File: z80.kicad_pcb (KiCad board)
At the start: 2 copper layers, 97.2 x 111.8 mm, 35 parts, among them P2 CONN_01X02, P3 Jumper, SW1 RESET, U1 Z80CPU, U2 DIP_OSCILLATOR, U3 ATF16V8CV

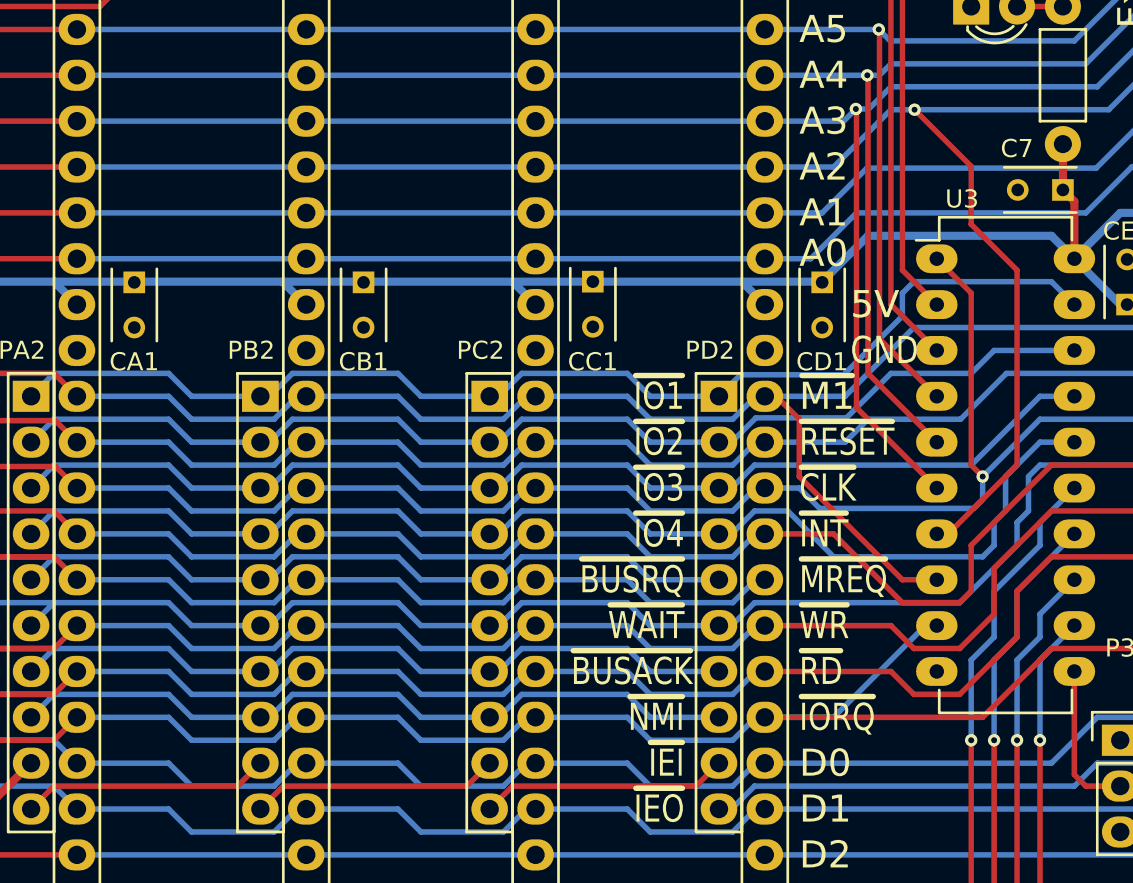
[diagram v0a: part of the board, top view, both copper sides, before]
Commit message: Added logo schematic elements and new logo for bottom side.
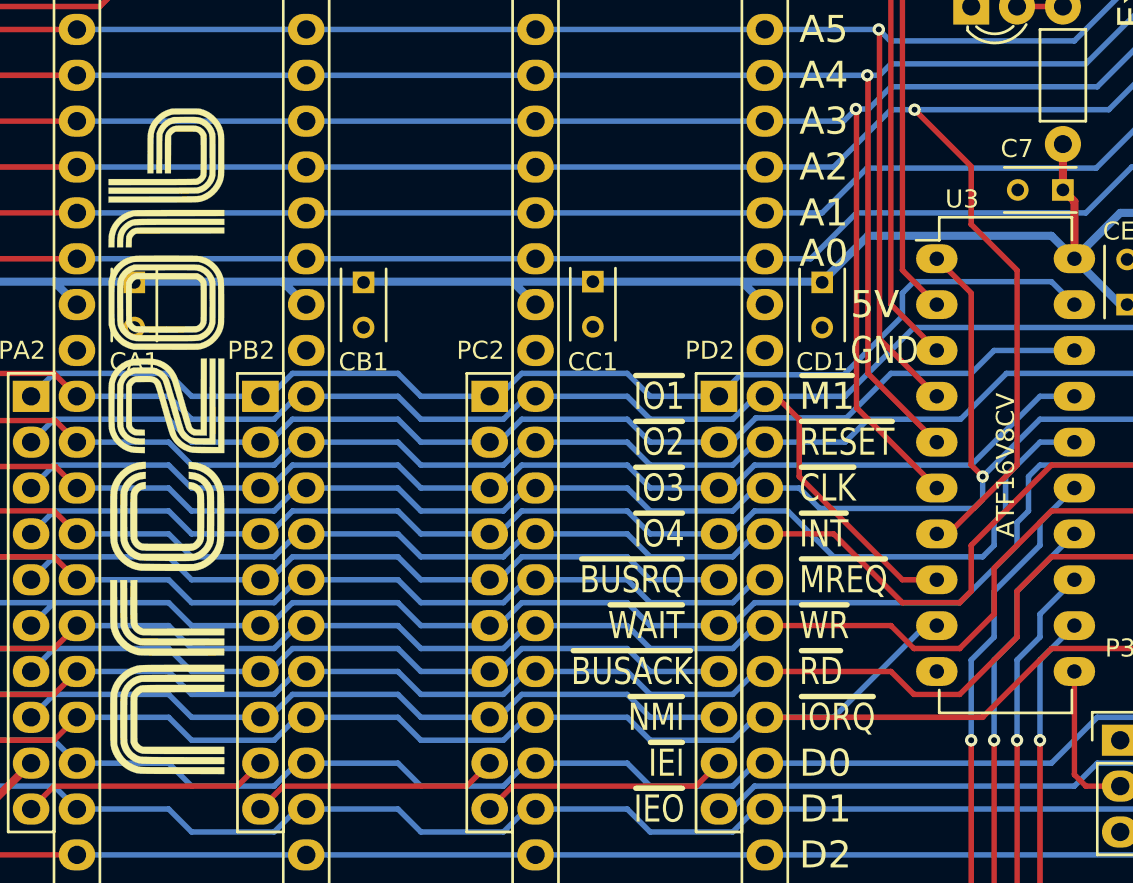
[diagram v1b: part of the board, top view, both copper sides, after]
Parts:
- added LOGO1: FrontLogo, ncr2016_logo:nrc2016_top_logo_1600, F.Cu at (78.7, 86.4)
- added LOGO2: BackLogo, ncr2016_logo:nrc2016_bottom_logo_600, B.Cu at (89.5, 85.1)
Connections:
- net /A0 renamed /CPU/A0
- net /A1 renamed /CPU/A1
- net /A10 renamed /CPU/A10
- net /A11 renamed /CPU/A11
- net /A12 renamed /CPU/A12
- net /A13 renamed /CPU/A13
- net /A14 renamed /CPU/A14
- net /A15 renamed /CPU/A15
- net /A2 renamed /CPU/A2
- net /A3 renamed /CPU/A3
- net /A4 renamed /CPU/A4
- net /A5 renamed /CPU/A5
- net /A6 renamed /CPU/A6
- net /A7 renamed /CPU/A7
- net /A8 renamed /CPU/A8
- net /A9 renamed /CPU/A9
- net /Card Slots/RX renamed /Card Slots/Expansion/RX
- net /Card Slots/S1 renamed /Card Slots/Expansion/SPARE1
- net /Card Slots/S2 renamed /Card Slots/Expansion/SPARE2
- net /Card Slots/S3 renamed /Card Slots/Expansion/SPARE3
- net /Card Slots/S4 renamed /Card Slots/PortA/SPARE4
- net /Card Slots/TX renamed /Card Slots/Expansion/TX
- net /Card Slots/~IOSEL0 renamed /Card Slots/PortA/~IOSEL0
- net /Card Slots/~IOSEL1 renamed /Card Slots/PortA/~IOSEL1
- net /Card Slots/~IOSEL2 renamed /Card Slots/PortA/~IOSEL2
- net /Card Slots/~IOSEL3 renamed /Card Slots/PortA/~IOSEL3
- net /D0 renamed /CPU/D0
- net /D1 renamed /CPU/D1
- net /D2 renamed /CPU/D2
- net /D3 renamed /CPU/D3
- net /D4 renamed /CPU/D4
- net /D5 renamed /CPU/D5
- net /D6 renamed /CPU/D6
- net /D7 renamed /CPU/D7
- net /~BUSACK renamed /CPU/~BUSACK
- net /~BUSRQ renamed /CPU/~BUSRQ
- net /~CLK renamed /CPU/~CLK
- net /~INT renamed /CPU/~INT
- net /~IORQ renamed /CPU/~IORQ
- net /~M1 renamed /CPU/~M1
- net /~MREQ renamed /CPU/~MREQ
- net /~NMI renamed /CPU/~NMI
- net /~RD renamed /CPU/~RD
- net /~RESET renamed /CPU/~RESET
- net /~WAIT renamed /CPU/~WAIT
- net /~WR renamed /CPU/~WR

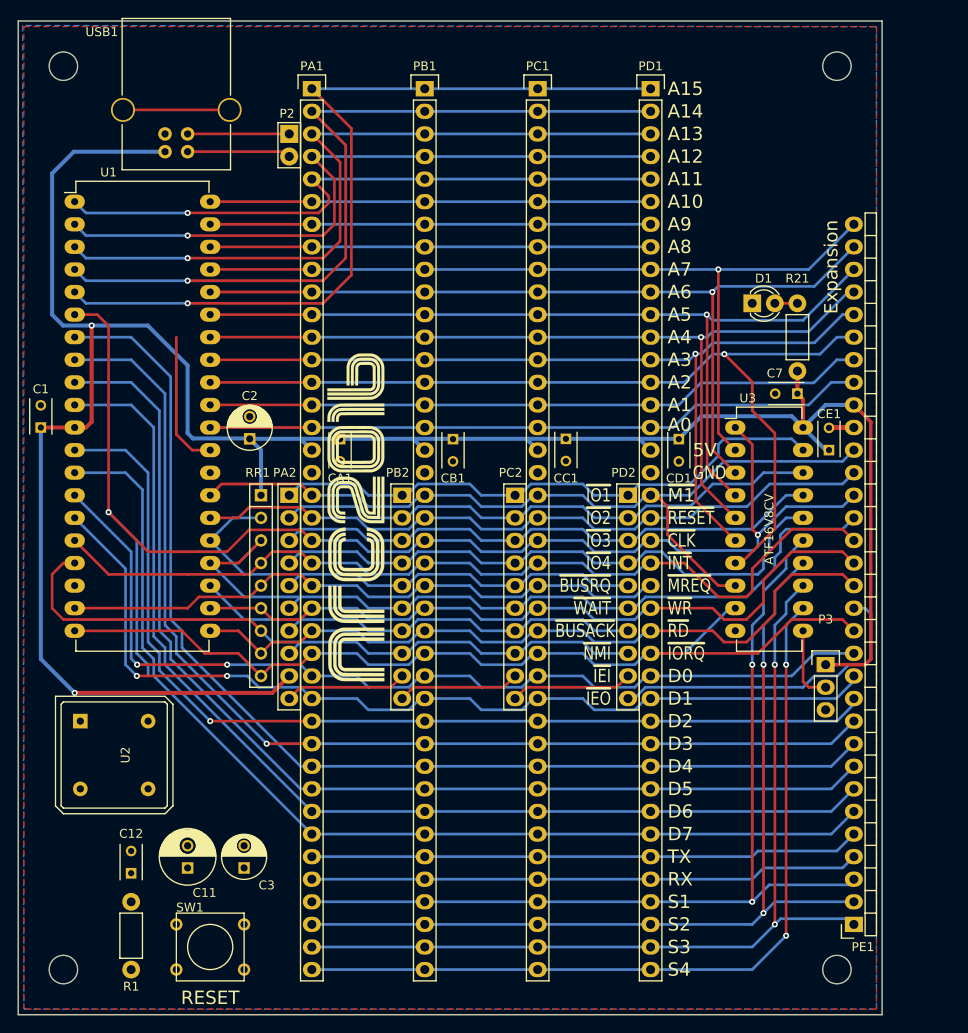
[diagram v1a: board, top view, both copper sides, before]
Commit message: * fixed DRC errors on pin 1 of Px2 connectors. * fixed unconnected ground pin issue of GAL. * added 8DIP and 14DIP oscillator block footprint. * updated bottom silkscreen. * added via stitching in a few places for better GND net. * routed the reset and oscillator circuits. * Design passes KiCAD DRC.
!! This is NRC016 RC1 !!
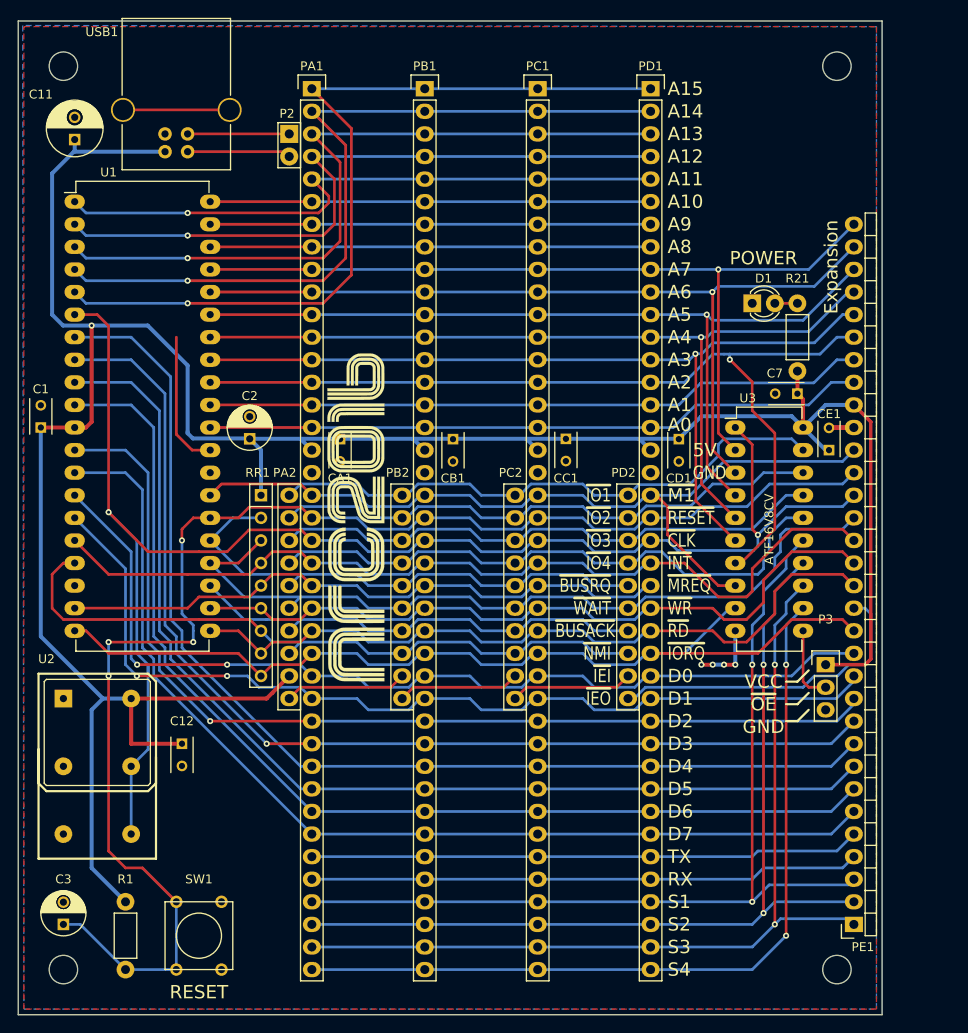
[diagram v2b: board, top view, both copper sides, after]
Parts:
- LOGO2: footprint ncr2016_logo:nrc2016_bottom_logo_600 -> ncr2016_logo:nrc2016_bottom_logo_600_v2
- PA2, PB2, PC2, PD2: footprint Socket_Strips:Socket_Strip_Straight_1x10 -> nrc2016:Socket_Strip_Straight_1x10_NRC2016
- U2: footprint Oscillators:OSC_DIP8 -> nrc2016:OSC_MULTIPACKAGE_DIP
- moved C11 82.9 mm to (47.0, 43.8)
- moved C3 21.3 mm to (45.7, 132.1)
- moved C12 15.6 mm to (59.1, 111.8), turned to 270 degrees
- moved U2 3.18 mm to (49.5, 110.5)
- moved SW1 1.80 mm to (61.0, 133.3), turned to 270 degrees
- moved R1 0.64 mm to (52.7, 129.5)
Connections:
- U3 pad 10: (no net) -> GND
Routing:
- net /CPU/~RESET: track 78.6 -> 161.0 mm, vias 0 -> 4
- net VCC: track 265.1 -> 301.3 mm, vias 2 -> 1
- net /CPU/~CLK: track 152.8 -> 172.6 mm
- net GND: track 21.2 -> 32.6 mm, vias 0 -> 4
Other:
- board text added: "POWER"
- board text added: "VCC"
- board text added: "~OE"

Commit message: Moved the slot a little further apart.
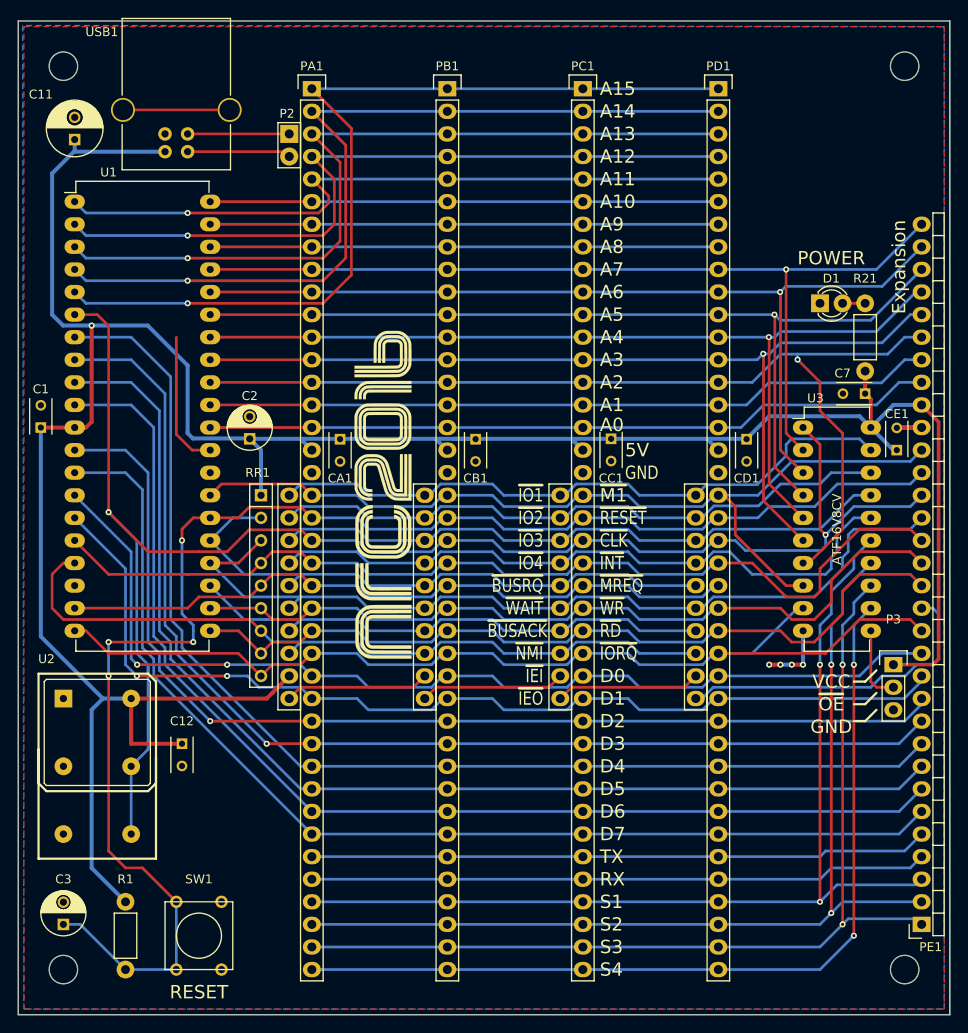
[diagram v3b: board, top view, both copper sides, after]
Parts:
- removed LOGO2: BackLogo, ncr2016_logo:nrc2016_bottom_logo_600_v2
- added G***: LOGO, ncr2016_logo:nrc2016_bottom_logo_600, B.Cu at (90.8, 85.7)
- moved CD1 7.62 mm to (122.6, 77.5)
- moved CE1 7.62 mm to (139.4, 78.7)
- moved D1 7.62 mm to (130.8, 62.2)
- moved MH2 7.62 mm to (140.3, 35.6)
- moved MH4 7.62 mm to (140.3, 137.2)
- moved P3 7.62 mm to (139.1, 102.9)
- moved PD2 7.62 mm to (116.8, 83.8)
- moved PE1 7.62 mm to (142.2, 132.1)
- moved U3 7.62 mm to (128.9, 76.2)
- moved PD1 7.62 mm to (119.4, 38.1)
- moved C7 7.62 mm to (135.9, 72.4)
- moved R21 7.62 mm to (135.9, 69.8)
- moved CC1 5.08 mm to (107.3, 77.5)
- moved PC1 5.08 mm to (104.1, 38.1)
- moved PC2 5.08 mm to (101.6, 83.8)
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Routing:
- net VCC: track 301.3 -> 311.5 mm
- net /CPU/A0: track 74.5 -> 82.8 mm
- net /CPU/D0: track 107.3 -> 114.9 mm
- net /CPU/~WAIT: track 91.2 -> 98.8 mm
- net /CPU/~RD: track 83.3 -> 91.0 mm
- net /CPU/~M1: track 94.3 -> 101.9 mm
- net /CPU/~IORQ: track 108.2 -> 115.8 mm
- net /CPU/A4: track 96.4 -> 104.0 mm
- net /Card Slots/PortA/~IOSEL2: track 63.0 -> 70.7 mm
- net /Card Slots/Expansion/TX: track 62.0 -> 69.6 mm
- net /CPU/~BUSRQ: track 59.8 -> 67.4 mm
- net /Card Slots/PortA/~IOSEL3: track 67.0 -> 74.6 mm
- net /Card Slots/PortA/~IOSEL1: track 63.0 -> 70.7 mm
- net /Card Slots/PortA/SPARE4: track 92.5 -> 100.2 mm
- net /Card Slots/Expansion/SPARE3: track 102.0 -> 109.6 mm
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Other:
- board size 97.2 x 111.8 mm -> 104.8 x 111.8 mm

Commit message: updated bottom logo.
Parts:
- removed G***: LOGO, ncr2016_logo:nrc2016_bottom_logo_600
- added LOGO2: BackLogo, ncr2016_logo:nrc2016_bottom_logo_600_v3, B.Cu at (93.2, 82.0)

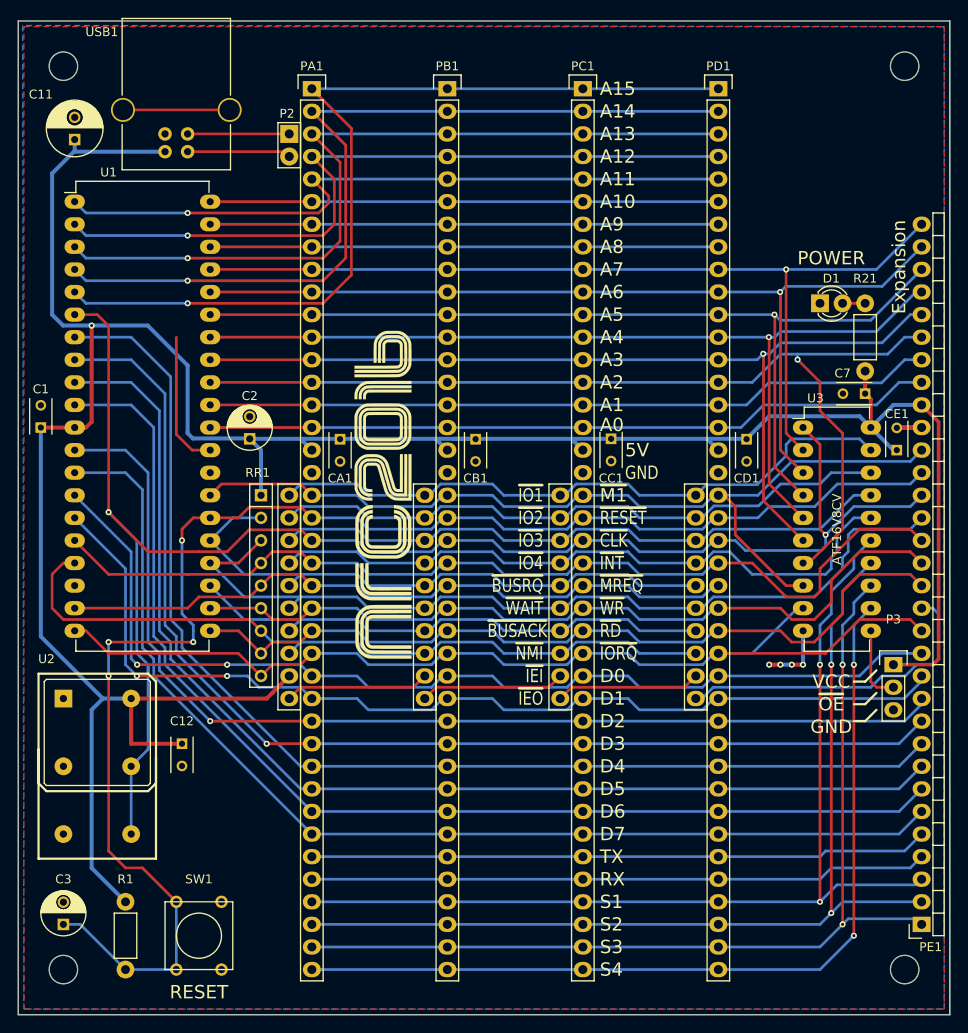
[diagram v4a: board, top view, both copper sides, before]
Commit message: fixed a VCC trace.
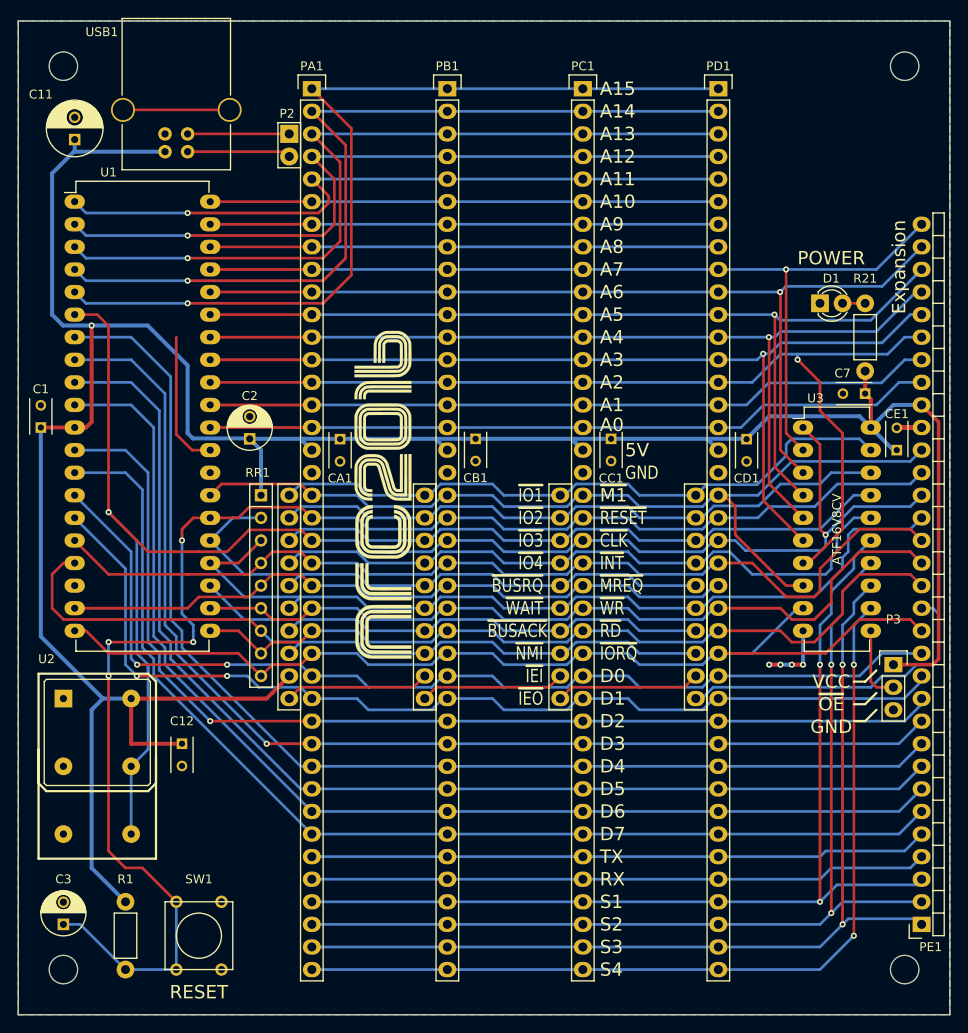
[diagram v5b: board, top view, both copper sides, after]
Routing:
- net VCC: track 311.5 -> 310.8 mm
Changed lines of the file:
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@@
   (general
     (links 290)
-    (no_connects 1)
+    (no_connects 0)
     (area 40.589999 30.429999 145.465001 142.290001)
     (thickness 1.6002)
     (drawings 68)
-    (tracks 904)
+    (tracks 905)
     (zones 0)
     (modules 37)
@@
     (0 Top signal hide)
     (31 Bottom signal hide)
-    (34 B.Paste user)
-    (35 F.Paste user)
+    (34 B.Paste user hide)
+    (35 F.Paste user hide)
     (36 B.SilkS user)
     (37 F.SilkS user)
-    (38 B.Mask user)
-    (39 F.Mask user)
-    (40 Dwgs.User user)
+    (38 B.Mask user hide)
+    (39 F.Mask user hide)
+    (40 Dwgs.User user hide)
     (44 Edge.Cuts user)
   )
@@
   )
   (module Capacitors_ThroughHole:C_Rect_L4_W2.5_P2.5 (layer Top)
-    (at 92.075 77.51 270)
+    (at 92.075 77.47 270)
     (descr "Film Capacitor Length 4mm x Width 2.5mm, Pitch 2.5mm")
     (tags Capacitor)
@@
   (gr_line (start 40.64 142.24) (end 40.64 30.48) (angle 90) (layer Edge.Cuts) (width 0.1))
   (gr_line (start 40.64 30.48) (end 145.415 30.48) (angle 90) (layer Edge.Cuts) (width 0.1))
+  (segment (start 92.075 77.47) (end 102.87 77.47) (width 0.45) (layer Bottom) (net 1) (status 400000))
+  (segment (start 102.87 77.47) (end 104.14 78.74) (width 0.45) (layer Bottom) (net 1) (status 800000))
+  (segment (start 104.14 78.74) (end 102.87 77.47) (width 0.45) (layer Bottom) (net 1))
   (segment (start 107.315 77.47) (end 118.11 77.47) (width 0.45) (layer Bottom) (net 1))
-  (segment (start 89.575 77.47) (end 102.87 77.47) (width 0.45) (layer Bottom) (net 1))
   (segment (start 76.835 77.51) (end 76.875 77.47) (width 0.45) (layer Bottom) (net 1))
   (segment (start 76.875 77.47) (end 87.63 77.47) (width 0.45) (layer Bottom) (net 1))
@@
   (segment (start 119.38 78.74) (end 118.11 77.47) (width 0.45) (layer Bottom) (net 1))
   (segment (start 102.87 77.47) (end 107.315 77.47) (width 0.45) (layer Bottom) (net 1))
-  (segment (start 104.14 78.74) (end 102.87 77.47) (width 0.45) (layer Bottom) (net 1))
   (segment (start 72.45684 77.47) (end 72.39 77.47) (width 0.45) (layer Bottom) (net 1))
   (segment (start 72.39 77.47) (end 66.717802 77.47) (width 0.45) (layer Bottom) (net 1))
@@
     (polygon
       (pts
-        (xy 41.148 30.988) (xy 41.275 141.605) (xy 144.78 141.605) (xy 144.78 31.115)
+        (xy 40.64 30.48) (xy 40.64 142.24) (xy 145.415 142.24) (xy 145.415 30.48)
       )
     )
@@
     (polygon
       (pts
-        (xy 41.275 31.115) (xy 144.78 31.115) (xy 144.78 141.605) (xy 41.275 141.605)
+        (xy 40.64 30.48) (xy 145.415 30.48) (xy 145.415 142.24) (xy 40.64 142.24)
       )
     )
